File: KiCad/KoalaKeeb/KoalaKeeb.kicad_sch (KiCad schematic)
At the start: 62 parts, among them J1 JLC_Battery_Con_L, J2 JLC_Battery_Con_R, SW1 Switch_SW_Push, SW10 Switch_SW_Push, SW11 Switch_SW_Push, SW12 Switch_SW_Push, SW13 Switch_SW_Push, SW14 Switch_SW_Push, SW15 Switch_SW_Push, SW16 Switch_SW_Push, SW17 Switch_SW_Push, SW18 Switch_SW_Push, SW19 Switch_SW_Push, SW2 Switch_SW_Push, SW20 Switch_SW_Push, SW21 Switch_SW_Push, SW22 Switch_SW_Push, SW23 Switch_SW_Push, SW24 Switch_SW_Push, SW25 Switch_SW_Push, SW26 Switch_SW_Push, SW27 Switch_SW_Push, SW28 Switch_SW_Push, SW29 Switch_SW_Push, SW3 Switch_SW_Push, SW30 Switch_SW_Push, SW31 Switch_SW_Push, SW32 Switch_SW_Push, SW33 Switch_SW_Push, SW34 Switch_SW_Push, SW4 Switch_SW_Push, SW5 Switch_SW_Push, SW6 Switch_SW_Push, SW7 Switch_SW_Push, SW8 Switch_SW_Push, SW9 Switch_SW_Push, U1 Nice!Nano_L, U2 Nice!Nano_R

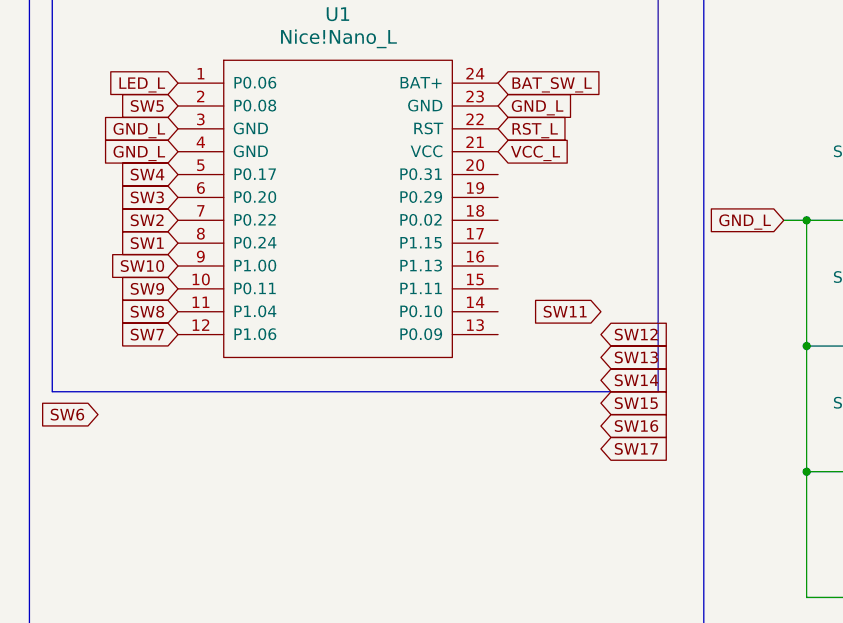
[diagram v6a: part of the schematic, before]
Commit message: update routing for right half LEDs
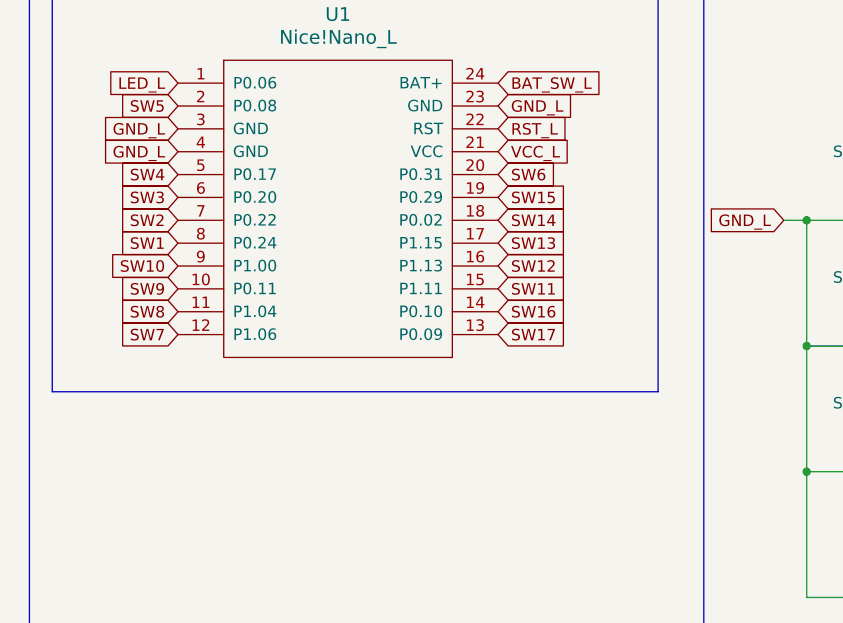
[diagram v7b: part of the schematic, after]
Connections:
- net SW11: now also U1.15 (P1.11)
- net SW12: now also U1.16 (P1.13)
- net SW13: now also U1.17 (P1.15)
- net SW14: now also U1.18 (P0.02)
- net SW15: now also U1.19 (P0.29)
- net SW16: now also U1.14 (P0.10)
- net SW17: now also U1.13 (P0.09)
- net SW6: now also U1.20 (P0.31)
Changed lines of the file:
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@@
     )
   )
-  (global_label "SW11" (shape input) (at 81.28 66.04 180) (fields_autoplaced)
-    (effects (font (size 1.27 1.27)) (justify right))
-    (property "Intersheetrefs" "${INTERSHEET_REFS}" (at 73.2149 66.04 0)
-      (effects (font (size 1.27 1.27)) (justify right) hide)
+  (global_label "SW11" (shape input) (at 69.85 63.5 0) (fields_autoplaced)
+    (effects (font (size 1.27 1.27)) (justify left))
+    (property "Intersheetrefs" "${INTERSHEET_REFS}" (at 77.9151 63.5 0)
+      (effects (font (size 1.27 1.27)) (justify left) hide)
     )
   )
@@
     )
   )
-  (global_label "SW13" (shape input) (at 81.28 71.12 0) (fields_autoplaced)
-    (effects (font (size 1.27 1.27)) (justify left))
-    (property "Intersheetrefs" "${INTERSHEET_REFS}" (at 89.3451 71.12 0)
+  (global_label "SW13" (shape input) (at 69.85 58.42 0) (fields_autoplaced)
+    (effects (font (size 1.27 1.27)) (justify left))
+    (property "Intersheetrefs" "${INTERSHEET_REFS}" (at 77.9151 58.42 0)
       (effects (font (size 1.27 1.27)) (justify left) hide)
     )
@@
     )
   )
-  (global_label "SW12" (shape input) (at 81.28 68.58 0) (fields_autoplaced)
-    (effects (font (size 1.27 1.27)) (justify left))
-    (property "Intersheetrefs" "${INTERSHEET_REFS}" (at 89.3451 68.58 0)
+  (global_label "SW12" (shape input) (at 69.85 60.96 0) (fields_autoplaced)
+    (effects (font (size 1.27 1.27)) (justify left))
+    (property "Intersheetrefs" "${INTERSHEET_REFS}" (at 77.9151 60.96 0)
       (effects (font (size 1.27 1.27)) (justify left) hide)
     )
@@
     )
   )
-  (global_label "SW6" (shape input) (at 25.4 77.47 180) (fields_autoplaced)
-    (effects (font (size 1.27 1.27)) (justify right))
-    (property "Intersheetrefs" "${INTERSHEET_REFS}" (at 18.5444 77.47 0)
-      (effects (font (size 1.27 1.27)) (justify right) hide)
+  (global_label "SW6" (shape input) (at 69.85 50.8 0) (fields_autoplaced)
+    (effects (font (size 1.27 1.27)) (justify left))
+    (property "Intersheetrefs" "${INTERSHEET_REFS}" (at 76.7056 50.8 0)
+      (effects (font (size 1.27 1.27)) (justify left) hide)
     )
   )
@@
     )
   )
-  (global_label "SW17" (shape input) (at 81.28 81.28 0) (fields_autoplaced)
-    (effects (font (size 1.27 1.27)) (justify left))
-    (property "Intersheetrefs" "${INTERSHEET_REFS}" (at 89.3451 81.28 0)
+  (global_label "SW17" (shape input) (at 69.85 68.58 0) (fields_autoplaced)
+    (effects (font (size 1.27 1.27)) (justify left))
+    (property "Intersheetrefs" "${INTERSHEET_REFS}" (at 77.9151 68.58 0)
       (effects (font (size 1.27 1.27)) (justify left) hide)
     )
@@
     )
   )
-  (global_label "SW15" (shape input) (at 81.28 76.2 0) (fields_autoplaced)
-    (effects (font (size 1.27 1.27)) (justify left))
-    (property "Intersheetrefs" "${INTERSHEET_REFS}" (at 89.3451 76.2 0)
+  (global_label "SW15" (shape input) (at 69.85 53.34 0) (fields_autoplaced)
+    (effects (font (size 1.27 1.27)) (justify left))
+    (property "Intersheetrefs" "${INTERSHEET_REFS}" (at 77.9151 53.34 0)
       (effects (font (size 1.27 1.27)) (justify left) hide)
     )
@@
     )
   )
-  (global_label "SW14" (shape input) (at 81.28 73.66 0) (fields_autoplaced)
-    (effects (font (size 1.27 1.27)) (justify left))
-    (property "Intersheetrefs" "${INTERSHEET_REFS}" (at 89.3451 73.66 0)
+  (global_label "SW14" (shape input) (at 69.85 55.88 0) (fields_autoplaced)
+    (effects (font (size 1.27 1.27)) (justify left))
+    (property "Intersheetrefs" "${INTERSHEET_REFS}" (at 77.9151 55.88 0)
       (effects (font (size 1.27 1.27)) (justify left) hide)
     )
@@
     )
   )
-  (global_label "SW16" (shape input) (at 81.28 78.74 0) (fields_autoplaced)
-    (effects (font (size 1.27 1.27)) (justify left))
-    (property "Intersheetrefs" "${INTERSHEET_REFS}" (at 89.3451 78.74 0)
-      (effects (font (size 1.27 1.27)) (justify left) hide)
-    )
+  (global_label "SW16" (shape input) (at 69.85 66.04 0) (fields_autoplaced)
+    (effects (font (size 1.27 1.27)) (justify left))
+    (property "Intersheetrefs" "${INTERSHEET_REFS}" (at 77.9151 66.04 0)
+      (effects (font (size 1.27 1.27)) (justify left) hide)
+    )
